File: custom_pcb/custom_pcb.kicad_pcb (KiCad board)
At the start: 2 copper layers, 285 x 152 mm, 313 parts, among them J1 USB_mini_micro_B, K0 KEYSW, K1 KEYSW, K10 KEYSW, K11 KEYSW, K12 KEYSW, K13 KEYSW, K14 KEYSW, K15 KEYSW, K16 KEYSW, K17 KEYSW, K18 KEYSW, K19 KEYSW, K2 KEYSW, K20 KEYSW, K21 KEYSW, K22 KEYSW, K23 KEYSW, K24 KEYSW, K25 KEYSW, K26 KEYSW, K27 KEYSW, K28 KEYSW, K29 KEYSW, K3 KEYSW, K30 KEYSW, K31 KEYSW, K32 KEYSW, K33 KEYSW, K34 KEYSW, K35 KEYSW, K36 KEYSW, K37 KEYSW, K38 KEYSW, K39 KEYSW, K4 KEYSW, K40 KEYSW, K41 KEYSW, K42 KEYSW, K43 KEYSW, K44 KEYSW, K45 KEYSW, K46 KEYSW, K47 KEYSW, K48 KEYSW, K49 KEYSW, K5 KEYSW, K50 KEYSW, K51 KEYSW, K52 KEYSW, K53 KEYSW, K54 KEYSW, K55 KEYSW, K56 KEYSW, K57 KEYSW, K58 KEYSW, K59 KEYSW, K6 KEYSW, K60 KEYSW, K63 KEYSW, K64 KEYSW, K65 KEYSW, K66 KEYSW, K67 KEYSW, K68 KEYSW, K69 KEYSW, K7 KEYSW, K70 KEYSW, K71 KEYSW, K72 KEYSW, K73 KEYSW, K74 KEYSW, K75 KEYSW, K76 KEYSW, K77 KEYSW, K78 KEYSW, K79 KEYSW, K8 KEYSW, K80 KEYSW, K81 KEYSW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

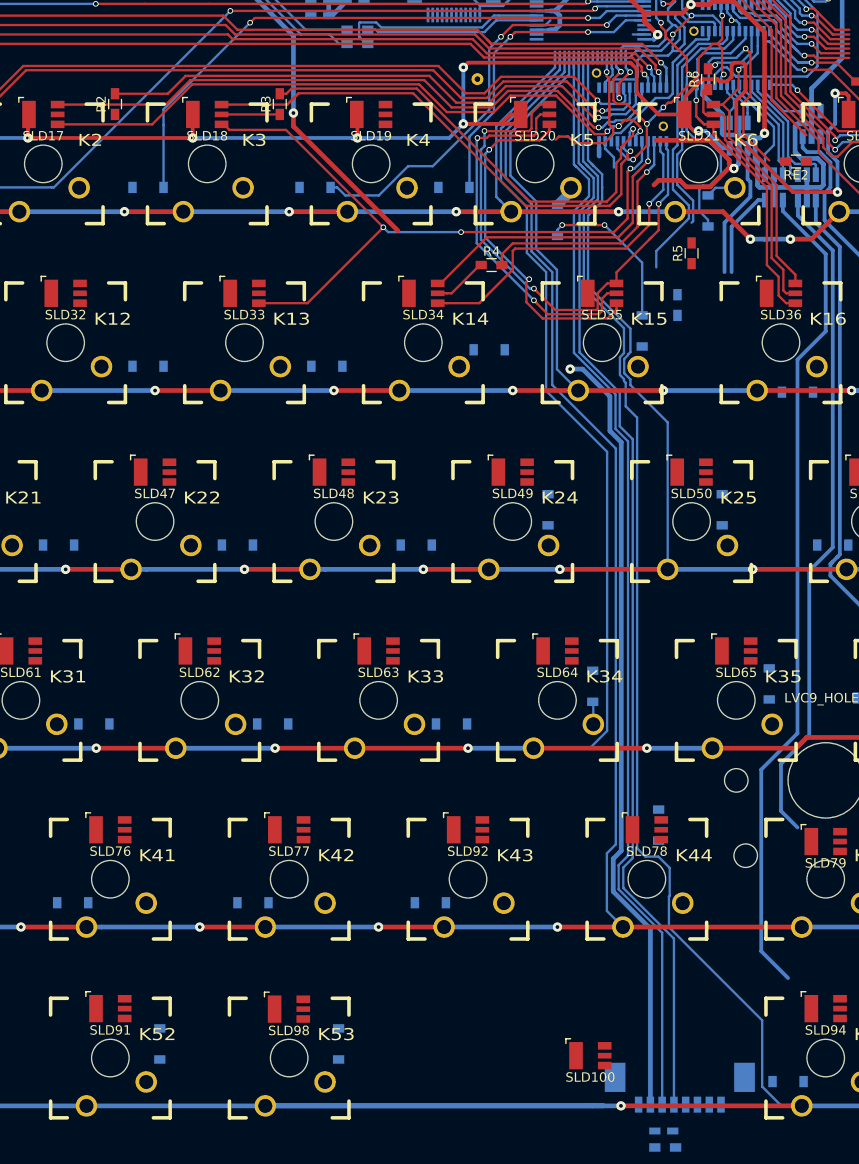
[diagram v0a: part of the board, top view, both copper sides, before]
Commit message: about the move the mcu a few units to the left to free up some space
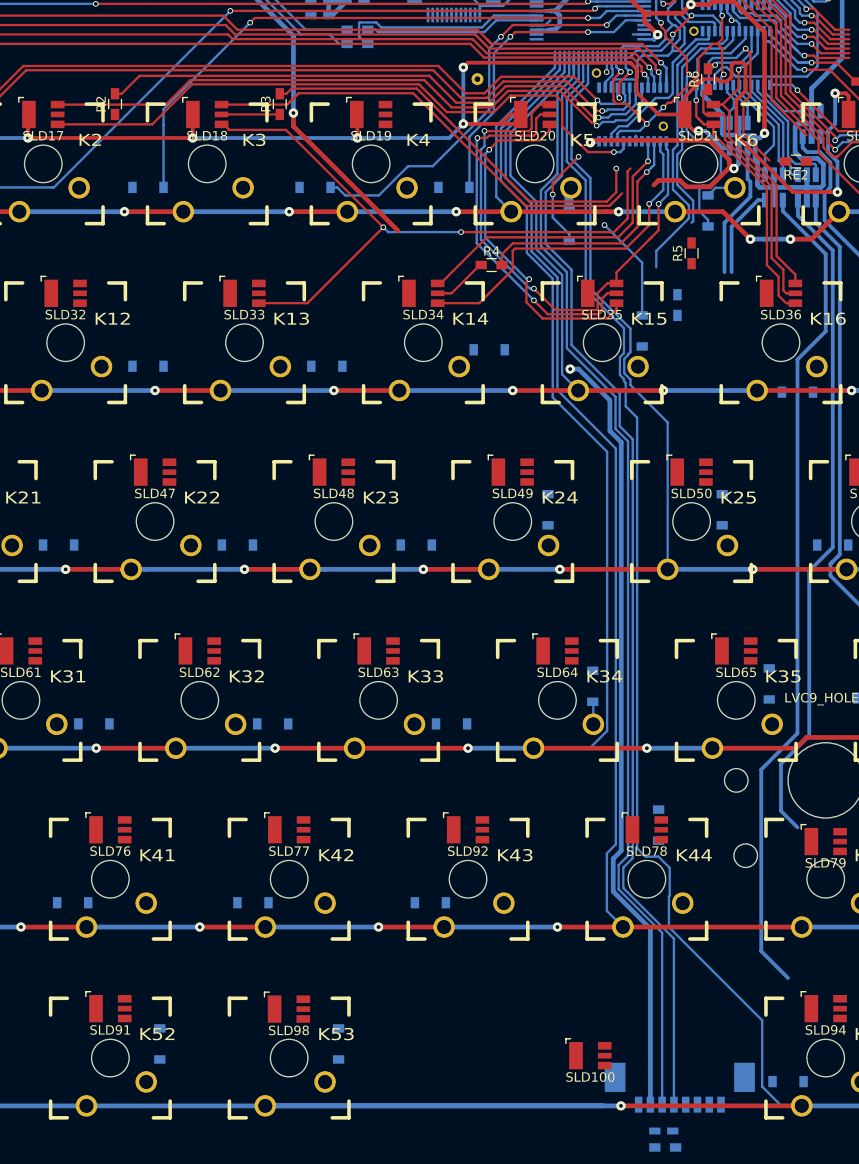
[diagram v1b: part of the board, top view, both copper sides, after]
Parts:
- moved D5 1.35 mm to (134.5, 60.5)
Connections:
- LC1 pad 18: green2 -> blue3
- LC1 pad 20: blue3 -> green2
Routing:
- net c5: track 33.6 -> 23.7 mm, vias 3 -> 4
- net +3V3: track 249.5 -> 256.0 mm, vias 9 -> 10
- net Net-(LC1-Pad19): track 50.3 -> 43.9 mm
- net blue3: track 56.7 -> 50.6 mm, vias 1 -> 0
- net green3: track 74.1 -> 70.5 mm, vias 3 -> 2
- net TP_CLK: track 118.8 -> 122.2 mm
- net Net-(LC1-Pad23): track 3.18 -> 0.00 mm
- net LED_OE: track 40.0 -> 37.1 mm, vias 6 -> 5
- net TP_DATA: track 117.8 -> 119.2 mm
- net Net-(D5-Pad2): track 7.82 -> 8.78 mm
- net green2: track 70.0 -> 69.1 mm, vias 4 -> 1

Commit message: progress!
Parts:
- moved U1 1.00 mm to (135.8, 37.0)
- moved V2 0.40 mm to (137.0, 44.4)
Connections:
- LC0 pad 20: (no net) -> OFF?
- LC2 pad 7: (no net) -> OFF?
- U1 pad 53: c5 -> (no net)
- U1 pad 56: (no net) -> c5
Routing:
- net c11: track 33.9 -> 0.00 mm, vias 1 -> 0
- net c12: track 33.4 -> 0.00 mm, vias 1 -> 0
- net GND: track 66.7 -> 94.1 mm, vias 0 -> 1
- net +3V3: track 256.0 -> 271.0 mm
- net Net-(U1-Pad32): track 4.26 -> 15.7 mm
- net c5: track 23.7 -> 33.1 mm, vias 4 -> 3
- net TP_CLK: track 122.2 -> 118.4 mm
- net OFF?: track 0.00 -> 3.62 mm, vias 0 -> 1
- net c14: track 30.1 -> 33.4 mm
- net LED_LE: track 33.3 -> 36.5 mm
- net c13: track 31.7 -> 33.9 mm
- net blue0: track 107.1 -> 105.4 mm
- net blue2: track 69.4 -> 68.0 mm
- net LED_OE: track 37.1 -> 35.8 mm
- net Net-(LC1-Pad7): track 61.8 -> 60.5 mm
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
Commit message: lots of fine routing work
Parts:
- moved V1 0.56 mm to (149.0, 33.8)
- moved Y0 0.27 mm to (144.0, 29.1)
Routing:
- net GND: track 94.1 -> 58.5 mm, vias 1 -> 0
- net c12: track 0.00 -> 34.8 mm, vias 0 -> 1
- net c11: track 0.00 -> 33.1 mm, vias 0 -> 1
- net +3V3: track 271.0 -> 244.8 mm, vias 10 -> 12
- net Net-(LC1-Pad23): track 0.00 -> 16.1 mm
- net Net-(U1-Pad32): track 15.7 -> 4.77 mm
- net Net-(U1-Pad24): track 0.00 -> 10.6 mm
- net Net-(U1-Pad22): track 0.00 -> 9.47 mm
- net green3: track 70.5 -> 74.3 mm, vias 2 -> 3
- net blue3: track 49.9 -> 53.1 mm, vias 0 -> 1
- net Net-(U1-Pad34): track 30.5 -> 27.3 mm
- net (no net): track 2.66 -> 0.00 mm
- net c14: track 33.4 -> 31.5 mm
- net green5: track 68.9 -> 67.2 mm
- net Net-(LC1-Pad19): track 43.9 -> 45.6 mm
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
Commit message: routing
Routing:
- net GND: track 58.5 -> 23.4 mm
- net as3: track 5.69 -> 8.99 mm
- net +3V3: track 244.8 -> 247.5 mm
- net green7: track 16.7 -> 18.7 mm
- net as5: track 11.2 -> 13.0 mm
- net blue8: track 10.9 -> 12.7 mm
- net as4: track 11.9 -> 13.4 mm
- net blue11: track 10.2 -> 11.5 mm
- net as2: track 11.5 -> 12.7 mm
- net as6: track 13.3 -> 14.1 mm

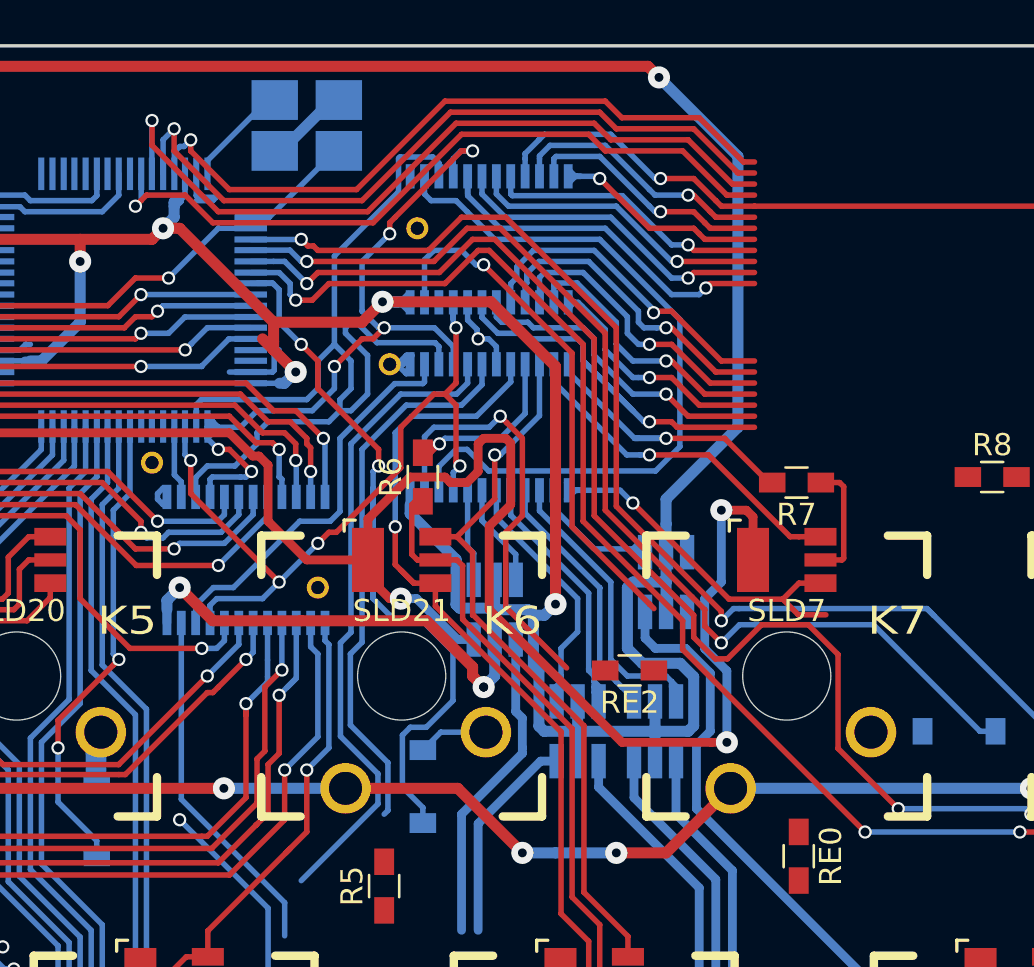
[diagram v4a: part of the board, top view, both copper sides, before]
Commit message: column routing
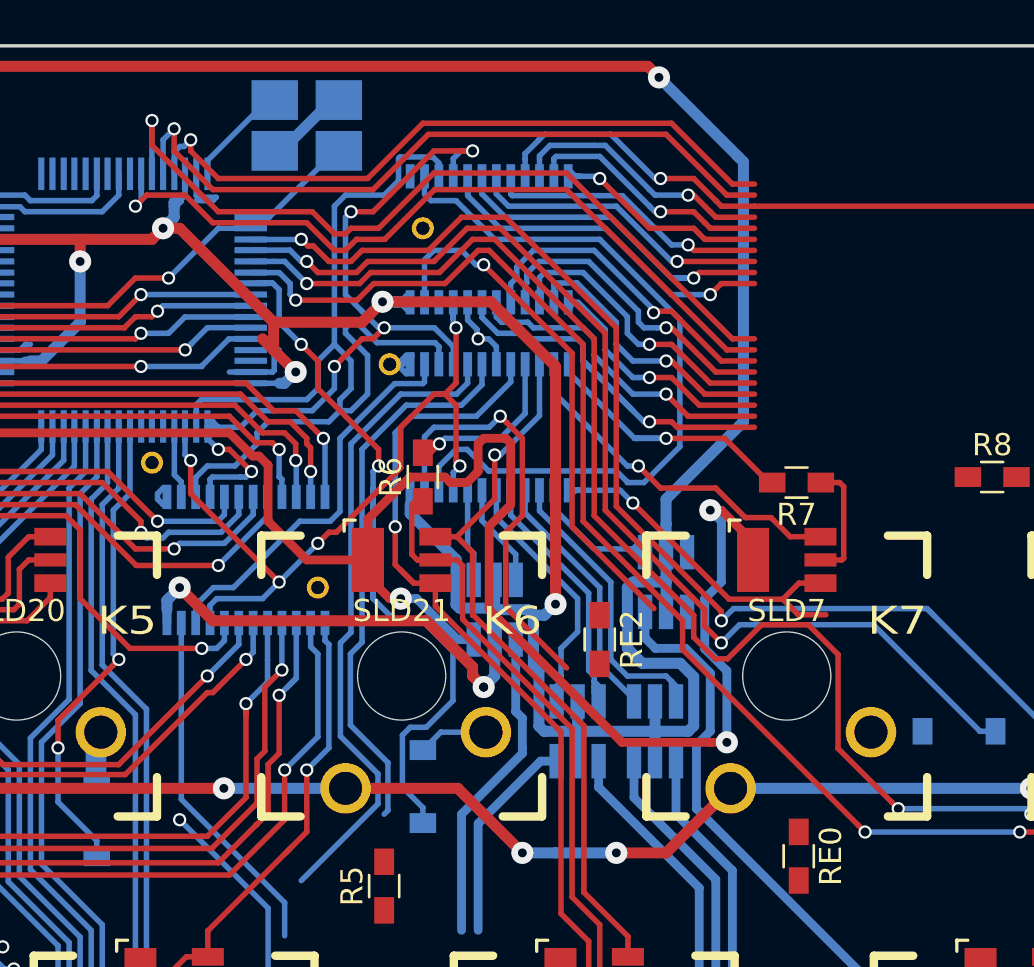
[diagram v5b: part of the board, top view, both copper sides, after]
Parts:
- moved RE2 1.94 mm to (157.2, 52.4), turned to 270 degrees
- moved V1 0.25 mm to (149.2, 33.8)
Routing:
- net LED_LE: track 36.9 -> 39.3 mm
- net c12: track 34.8 -> 36.7 mm
- net c11: track 33.1 -> 35.0 mm
- net as4: track 13.4 -> 11.6 mm
- net LED_CLK: track 44.3 -> 45.3 mm
- net c14: track 31.5 -> 30.6 mm
- net c13: track 33.2 -> 32.4 mm
- net blue10: track 14.8 -> 15.6 mm

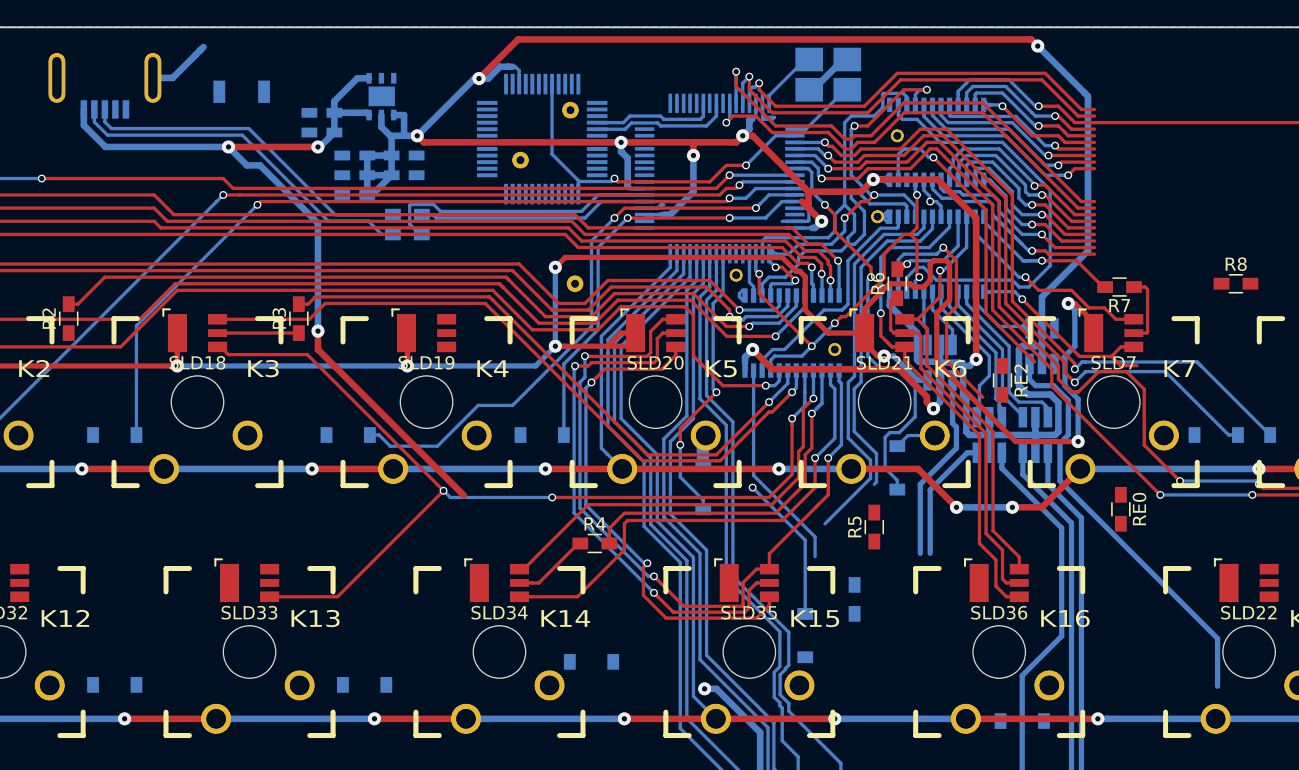
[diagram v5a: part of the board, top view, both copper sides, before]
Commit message: found a better way to get power and anodes around
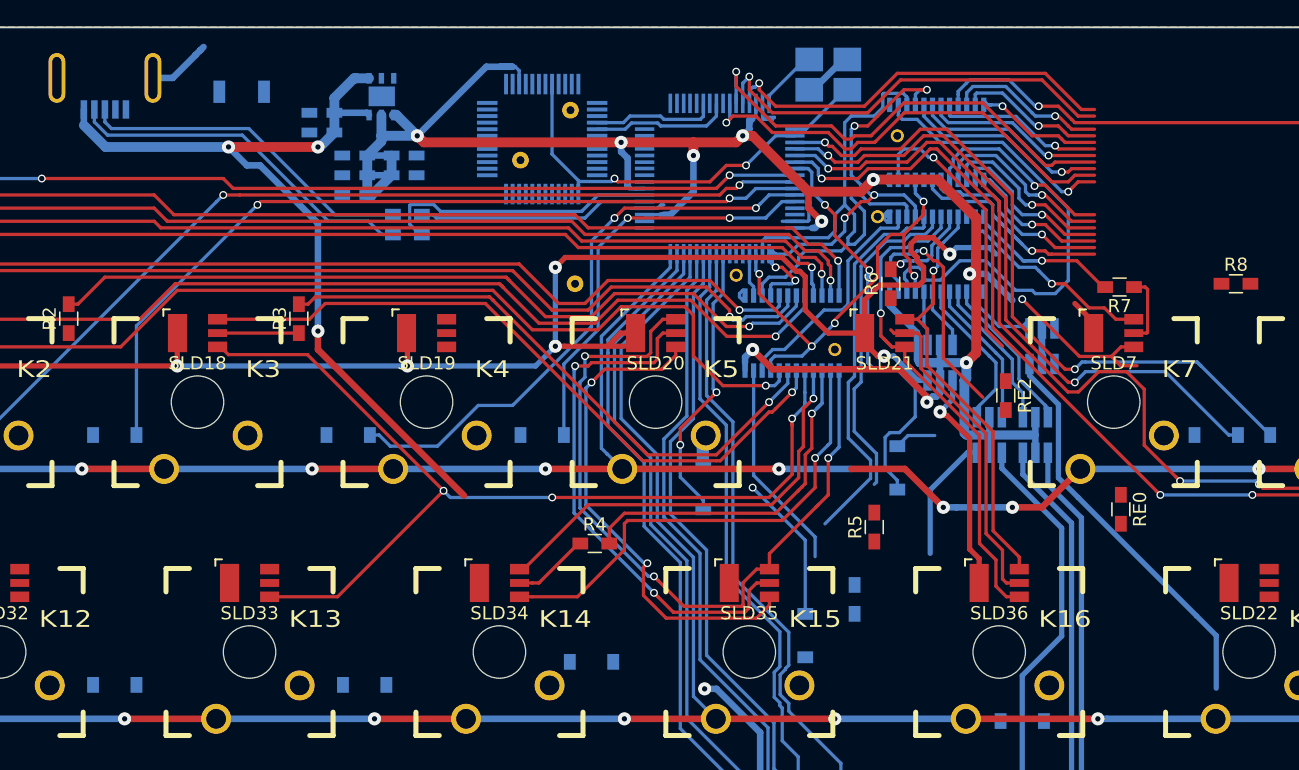
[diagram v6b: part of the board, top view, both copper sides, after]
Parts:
- removed K6: KEYSW, cherry_rgb:CHERRY_PLATE_91.6H
- moved RE2 1.18 mm to (157.5, 53.5)
- moved R6 0.50 mm to (148.8, 45.0)
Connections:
- LC2 pad 10: blue6 -> OFF?
- LC2 pad 7: OFF? -> green6
- LC2 pad 8: green6 -> Net-(LC2-Pad8)
- LC2 pad 9: Net-(LC2-Pad9) -> blue6
- R6 pad 2: Net-(LC2-Pad9) -> Net-(LC2-Pad8)
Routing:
- net +3V3: track 247.7 -> 176.0 mm, vias 12 -> 10
- net anode0: track 193.7 -> 168.5 mm, vias 9 -> 8
- net Net-(LC2-Pad9): track 9.40 -> 0.00 mm, vias 1 -> 0
- net Net-(LC2-Pad8): track 0.00 -> 7.33 mm, vias 0 -> 1
- net green7: track 18.7 -> 12.8 mm
- net LED_DATA2: track 34.1 -> 39.0 mm
- net c6: track 37.2 -> 32.6 mm
- net OFF?: track 3.62 -> 0.00 mm, vias 1 -> 0
- net red6: track 27.7 -> 24.9 mm
- net anode1: track 14.4 -> 17.2 mm, vias 0 -> 1
- net Net-(LC0-Pad23): track 23.8 -> 21.6 mm
- net as5: track 13.0 -> 11.2 mm
- net LED_OE: track 35.8 -> 37.2 mm
- net anode3: track 31.7 -> 30.5 mm
- net Net-(LC2-Pad23): track 19.9 -> 18.7 mm
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
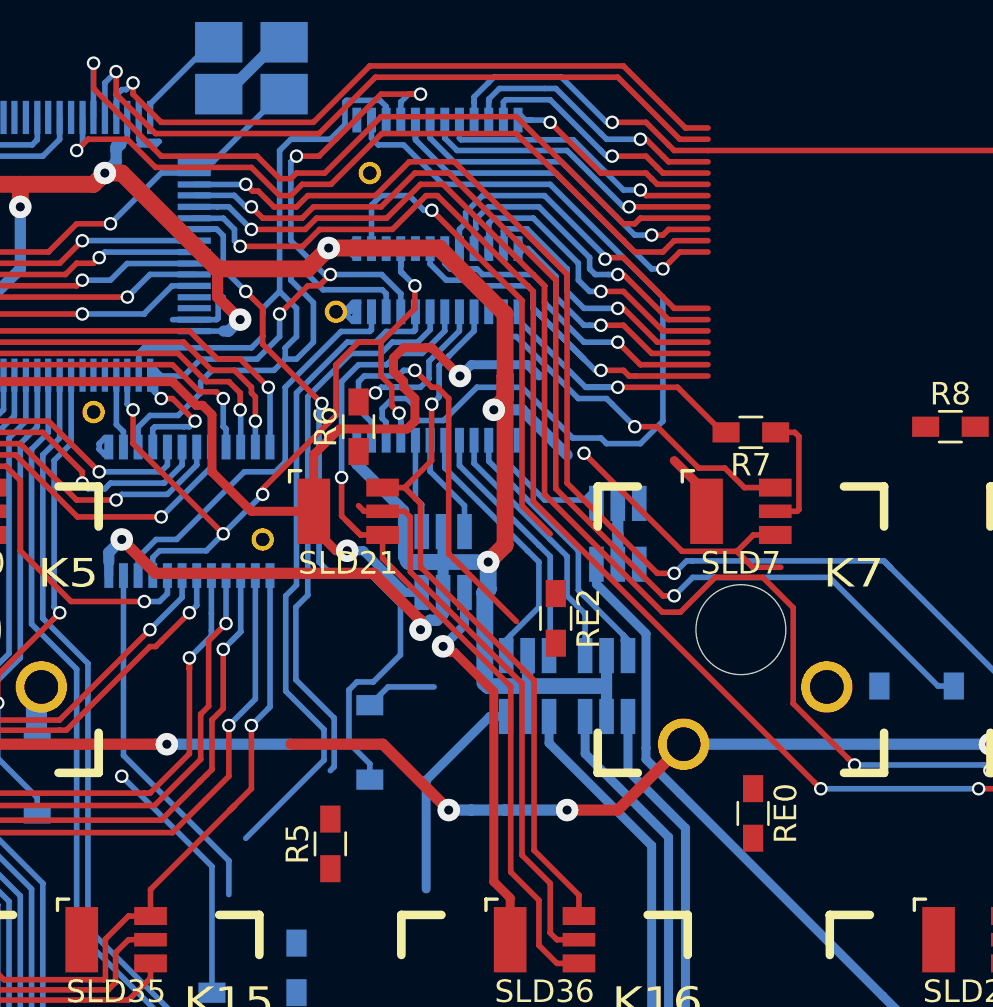
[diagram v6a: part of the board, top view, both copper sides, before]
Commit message: compacted routing
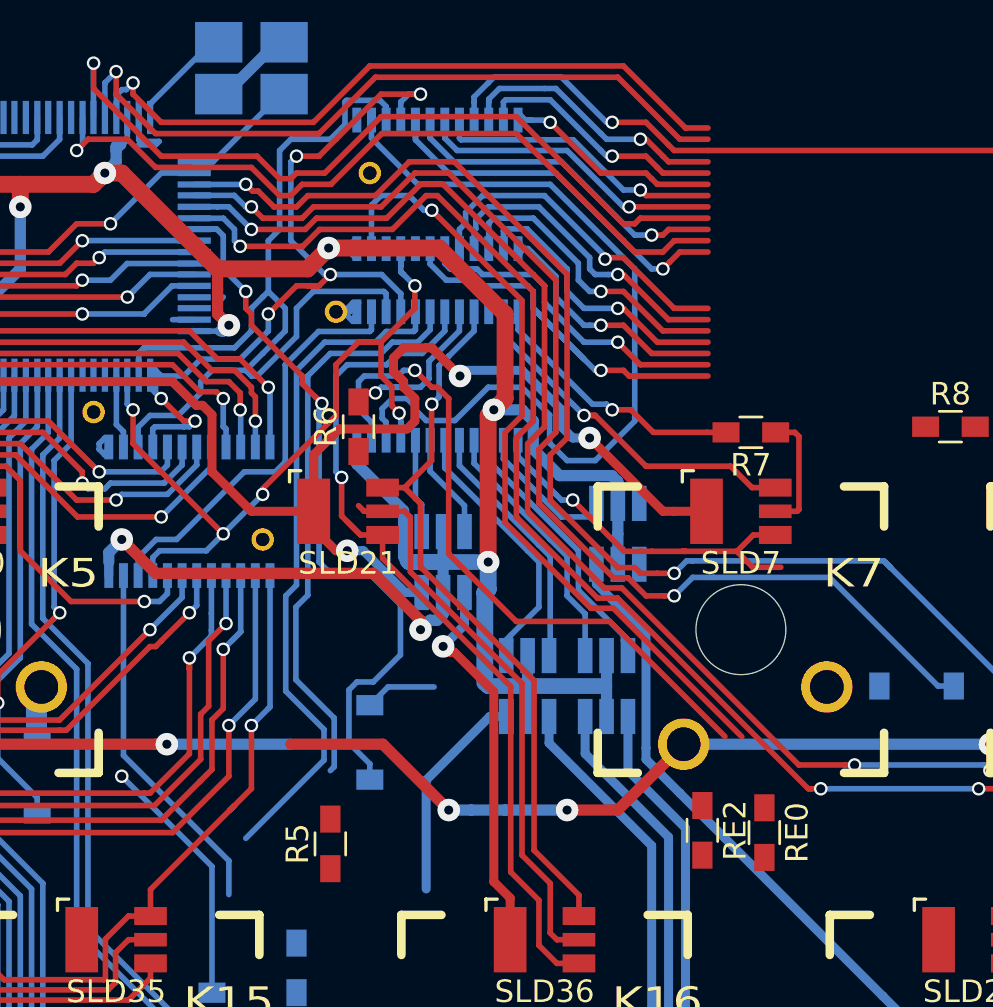
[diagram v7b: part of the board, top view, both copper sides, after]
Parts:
- moved RE2 11.4 mm to (164.0, 62.9)
- moved RE0 0.99 mm to (166.8, 63.0)
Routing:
- net Net-(LC0-Pad23): track 21.6 -> 35.3 mm
- net Net-(LC2-Pad23): track 18.7 -> 30.1 mm
- net anode0: track 168.5 -> 176.6 mm, vias 8 -> 9
- net green7: track 12.8 -> 16.6 mm
- net as3: track 8.99 -> 6.44 mm
- net LED_CLK: track 45.3 -> 42.8 mm
- net +3V3: track 176.0 -> 178.4 mm
- net c9: track 99.7 -> 97.4 mm
- net GND: track 23.4 -> 21.6 mm
- net c8: track 53.2 -> 54.7 mm
- net c10: track 114.7 -> 116.2 mm
- net c7: track 50.5 -> 51.9 mm
- net Net-(LC2-Pad12): track 13.0 -> 12.3 mm
- net LED_DATA2: track 39.0 -> 38.4 mm
- net green5: track 67.2 -> 67.7 mm
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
